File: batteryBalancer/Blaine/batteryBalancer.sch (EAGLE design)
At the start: 32 parts

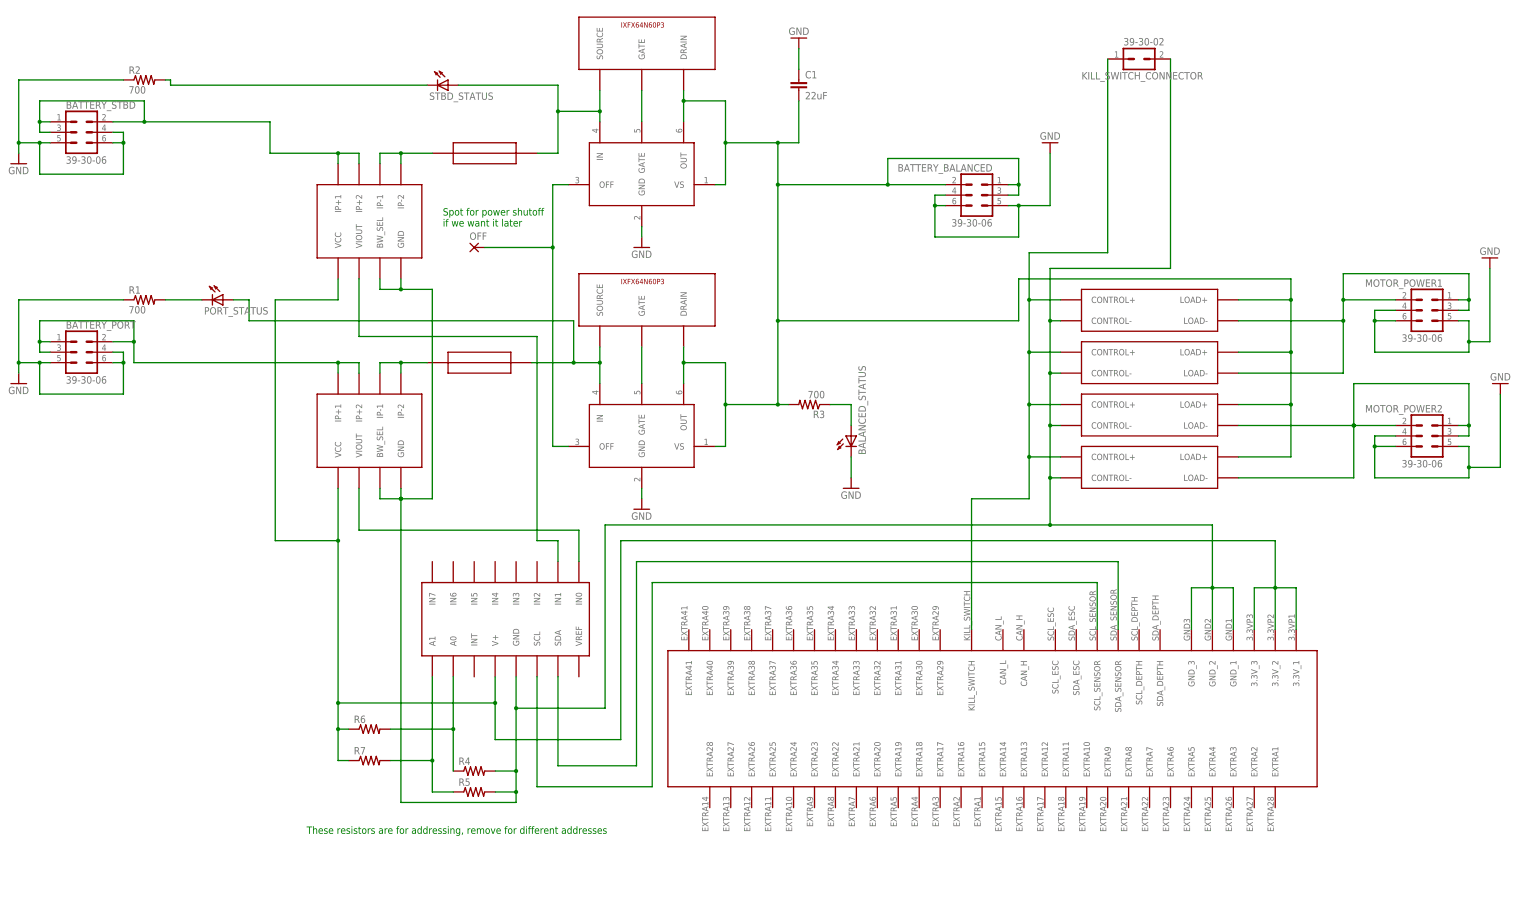
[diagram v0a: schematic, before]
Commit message: Routed the board
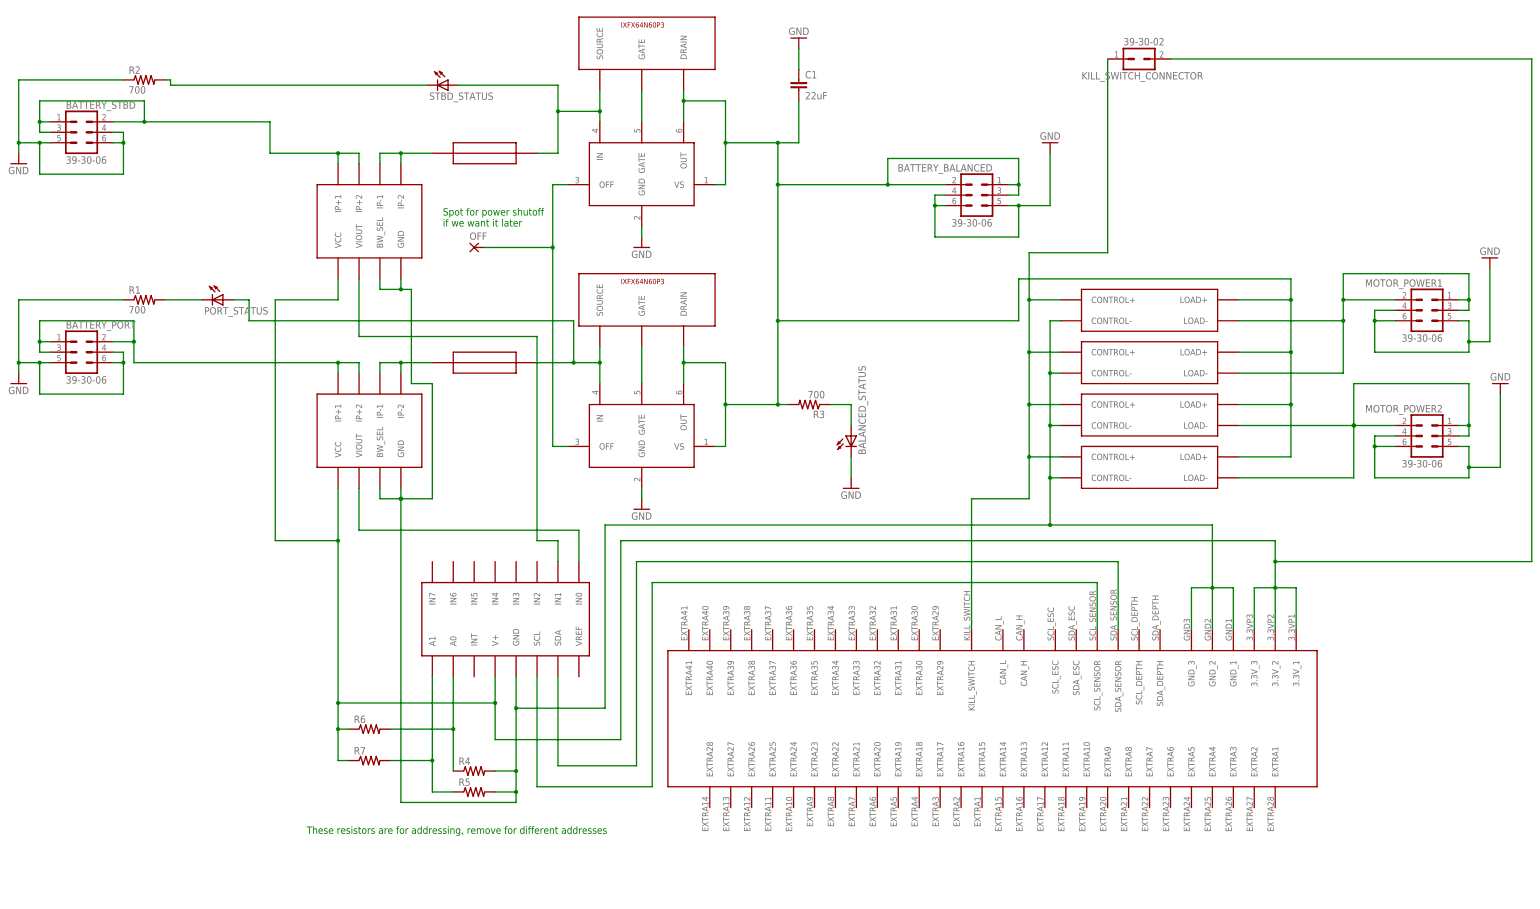
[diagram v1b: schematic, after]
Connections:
- net 3.3V: now also KILL_SWITCH_CONNECTOR.2
- net LOGIC_GND: no longer KILL_SWITCH_CONNECTOR.2
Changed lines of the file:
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@@
 <instance part="GND9" gate="1" x="396.24" y="149.86" rot="R180"/>
 <instance part="STBD_FUSE" gate="G$1" x="149.86" y="205.74"/>
-<instance part="PORT_FUSE" gate="G$1" x="148.59" y="154.94"/>
+<instance part="PORT_FUSE" gate="G$1" x="149.86" y="154.94"/>
 <instance part="ADC" gate="G$1" x="154.94" y="93.98"/>
 <instance part="R4" gate="G$1" x="147.32" y="55.88"/>
@@
 <junction x="157.48" y="55.88"/>
 <pinref part="PORT_CS" gate="G$1" pin="GND"/>
-<pinref part="STBD_CS" gate="G$1" pin="GND"/>
-<wire x1="129.54" y1="172.72" x2="129.54" y2="175.26" width="0.1524" layer="91"/>
-<pinref part="STBD_CS" gate="G$1" pin="BW_SEL"/>
-<wire x1="124.46" y1="175.26" x2="124.46" y2="172.72" width="0.1524" layer="91"/>
-<wire x1="124.46" y1="172.72" x2="129.54" y2="172.72" width="0.1524" layer="91"/>
-<junction x="129.54" y="172.72"/>
-<wire x1="137.16" y1="172.72" x2="129.54" y2="172.72" width="0.1524" layer="91"/>
-<wire x1="137.16" y1="121.92" x2="137.16" y2="172.72" width="0.1524" layer="91"/>
 <wire x1="157.48" y1="48.26" x2="129.54" y2="48.26" width="0.1524" layer="91"/>
 <wire x1="129.54" y1="48.26" x2="129.54" y2="121.92" width="0.1524" layer="91"/>
@@
 <wire x1="326.39" y1="115.57" x2="326.39" y2="100.33" width="0.1524" layer="91"/>
 <junction x="287.02" y="115.57"/>
-<wire x1="287.02" y1="165.1" x2="287.02" y2="177.8" width="0.1524" layer="91"/>
-<pinref part="KILL_SWITCH_CONNECTOR" gate="G$1" pin="2"/>
-<wire x1="287.02" y1="177.8" x2="316.23" y2="177.8" width="0.1524" layer="91"/>
-<wire x1="316.23" y1="177.8" x2="316.23" y2="228.6" width="0.1524" layer="91"/>
-<junction x="287.02" y="165.1"/>
+<wire x1="137.16" y1="121.92" x2="137.16" y2="149.86" width="0.1524" layer="91"/>
+<pinref part="STBD_CS" gate="G$1" pin="GND"/>
+<wire x1="129.54" y1="172.72" x2="129.54" y2="175.26" width="0.1524" layer="91"/>
+<junction x="129.54" y="172.72"/>
+<pinref part="STBD_CS" gate="G$1" pin="BW_SEL"/>
+<wire x1="132.08" y1="172.72" x2="129.54" y2="172.72" width="0.1524" layer="91"/>
+<wire x1="124.46" y1="175.26" x2="124.46" y2="172.72" width="0.1524" layer="91"/>
+<wire x1="124.46" y1="172.72" x2="129.54" y2="172.72" width="0.1524" layer="91"/>
+<wire x1="137.16" y1="149.86" x2="132.08" y2="149.86" width="0.1524" layer="91"/>
+<wire x1="132.08" y1="149.86" x2="132.08" y2="172.72" width="0.1524" layer="91"/>
 </segment>
 </net>
@@
 <wire x1="129.54" y1="154.94" x2="129.54" y2="152.4" width="0.1524" layer="91"/>
 <pinref part="PORT_FUSE" gate="G$1" pin="P$1"/>
-<wire x1="129.54" y1="154.94" x2="135.89" y2="154.94" width="0.1524" layer="91"/>
+<wire x1="129.54" y1="154.94" x2="137.16" y2="154.94" width="0.1524" layer="91"/>
 <junction x="129.54" y="154.94"/>
 </segment>
@@
 <wire x1="346.71" y1="100.33" x2="346.71" y2="90.17" width="0.1524" layer="91"/>
 <pinref part="EDGE_CONNECTOR" gate="G$1" pin="3.3V_2"/>
-<wire x1="341.63" y1="100.33" x2="341.63" y2="111.76" width="0.1524" layer="91"/>
+<wire x1="341.63" y1="100.33" x2="341.63" y2="106.68" width="0.1524" layer="91"/>
+<wire x1="341.63" y1="106.68" x2="341.63" y2="111.76" width="0.1524" layer="91"/>
 <wire x1="341.63" y1="100.33" x2="341.63" y2="90.17" width="0.1524" layer="91"/>
 <wire x1="341.63" y1="100.33" x2="346.71" y2="100.33" width="0.1524" layer="91"/>
@@
 <junction x="152.4" y="72.39"/>
 <junction x="114.3" y="72.39"/>
+<wire x1="341.63" y1="106.68" x2="403.86" y2="106.68" width="0.1524" layer="91"/>
+<wire x1="403.86" y1="106.68" x2="403.86" y2="228.6" width="0.1524" layer="91"/>
+<junction x="341.63" y="106.68"/>
+<pinref part="KILL_SWITCH_CONNECTOR" gate="G$1" pin="2"/>
+<wire x1="403.86" y1="228.6" x2="316.23" y2="228.6" width="0.1524" layer="91"/>
 </segment>
 </net>
@@
 <pinref part="PORT_FUSE" gate="G$1" pin="P$2"/>
 <wire x1="177.8" y1="154.94" x2="177.8" y2="149.86" width="0.1524" layer="91"/>
-<wire x1="161.29" y1="154.94" x2="171.45" y2="154.94" width="0.1524" layer="91"/>
+<wire x1="162.56" y1="154.94" x2="171.45" y2="154.94" width="0.1524" layer="91"/>
 <junction x="177.8" y="154.94"/>
 <pinref part="PORT_STATUS" gate="G$1" pin="A"/>

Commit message: Prettied up the routing and added kill switch indicator
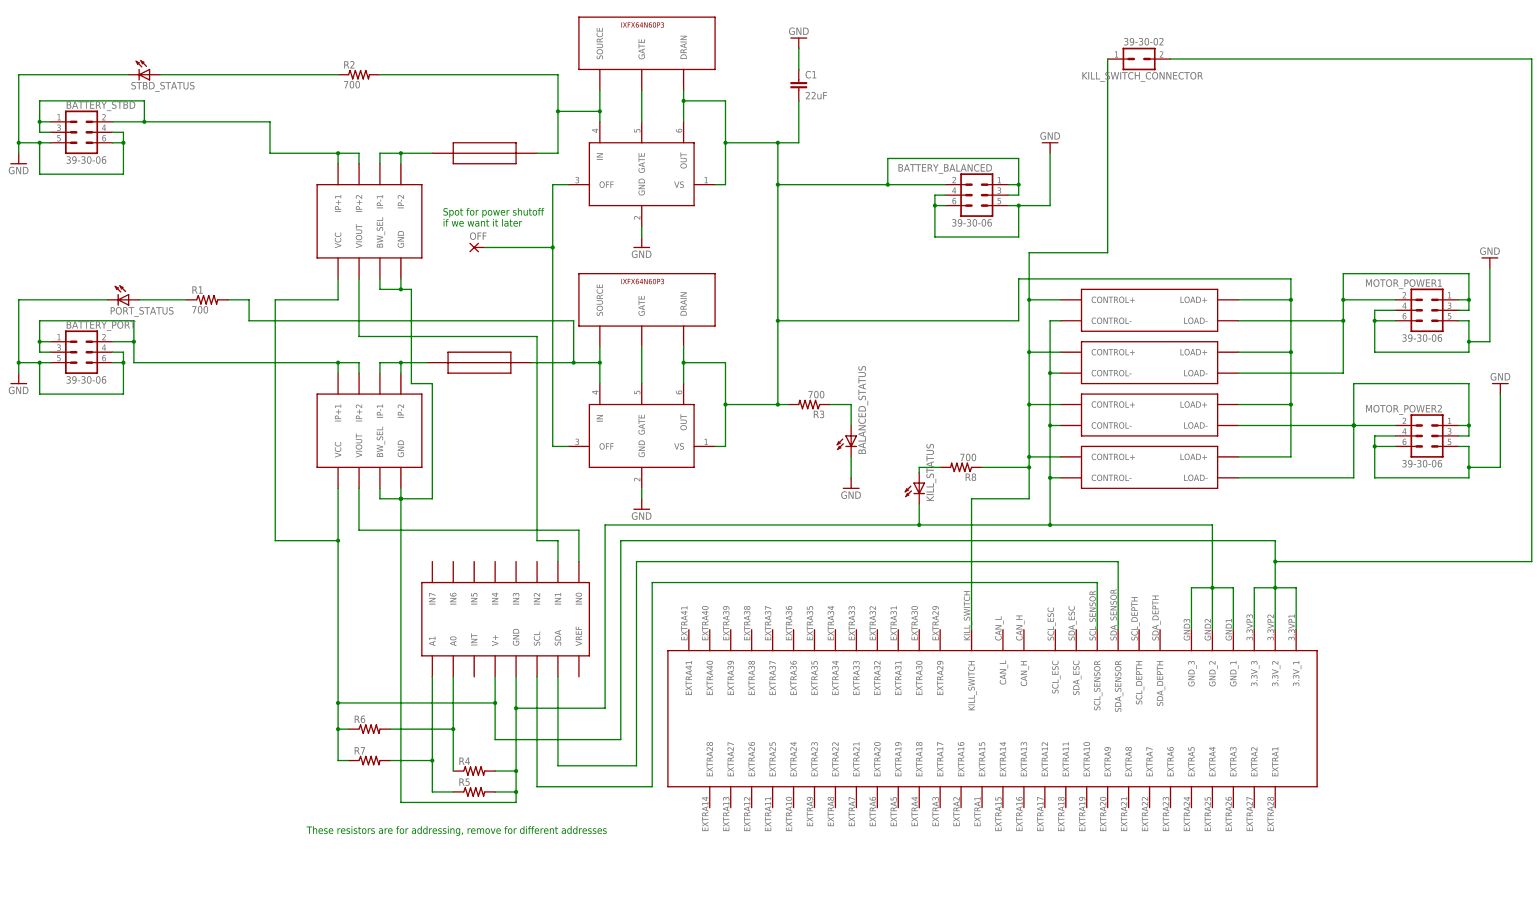
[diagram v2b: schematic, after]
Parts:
- added KILL_STATUS: LTST-S270GKT, LTST-S270GKT:LTST-S270GKT
- added R8: 700, rcl:R-US_0207/7
- R1, R2, R3: device rcl:R-US_MELF0204W -> rcl:R-US_0207/7
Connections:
- removed net PORT_INDICATOR: PORT_STATUS.C, R1.2
- removed net STBD_INDICATOR: R2.2, STBD_STATUS.C
- new net N$3: KILL_STATUS.A, R8.2
- new net PORT_STATUS: PORT_STATUS.A, R1.1
- new net STBD_STATUS: R2.1, STBD_STATUS.A
- net GND: now also PORT_STATUS.C, STBD_STATUS.C; no longer R1.1, R2.1
- net KILL_SWITCH: now also R8.1
- net LOGIC_GND: now also KILL_STATUS.C
- net N$1: now also R1.2; no longer PORT_STATUS.A
- net STBD_UNBALANCED: now also R2.2; no longer STBD_STATUS.A
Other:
- moved on the sheet: PORT_STATUS, R1, R2, STBD_STATUS

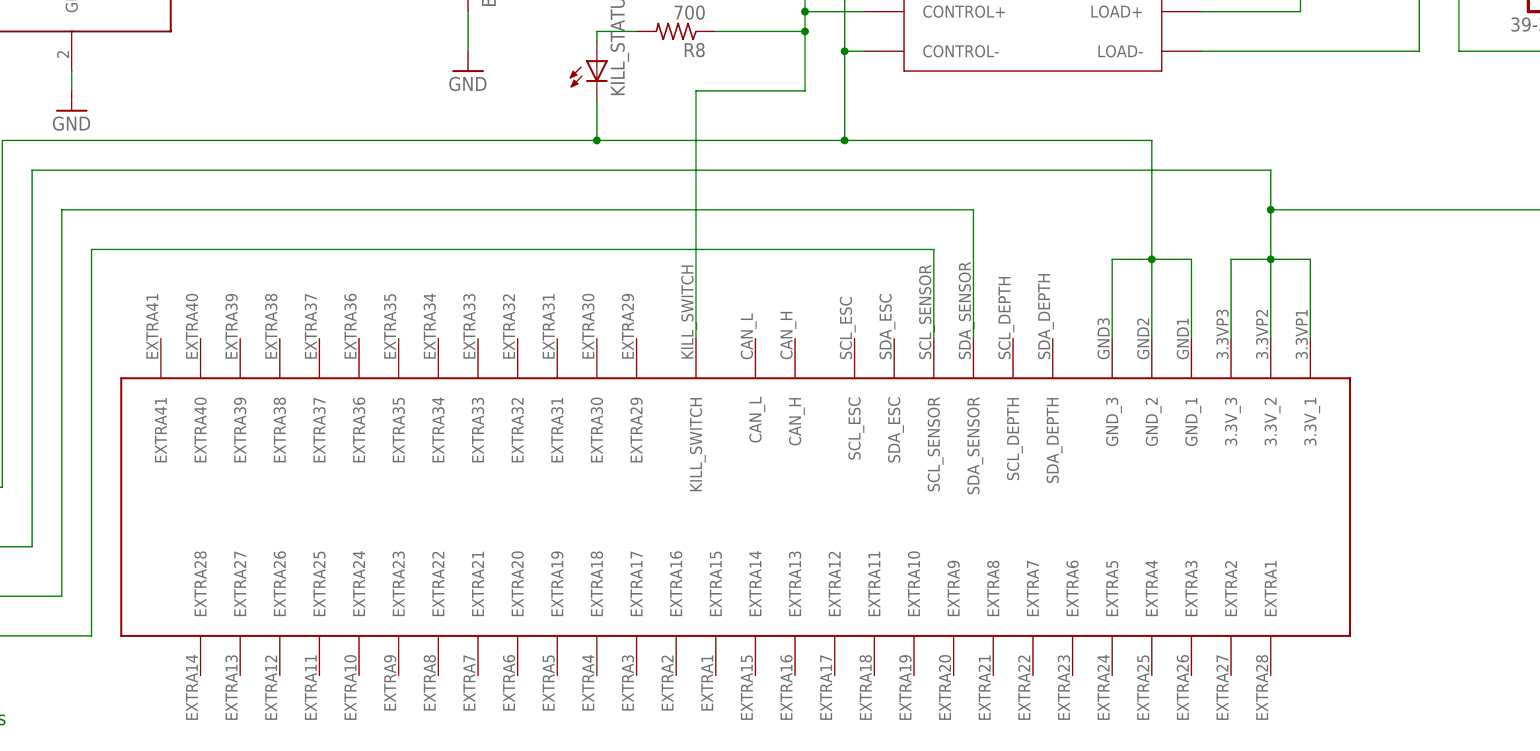
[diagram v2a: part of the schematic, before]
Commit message: Lost all my work :( but at least I got the new edge connector
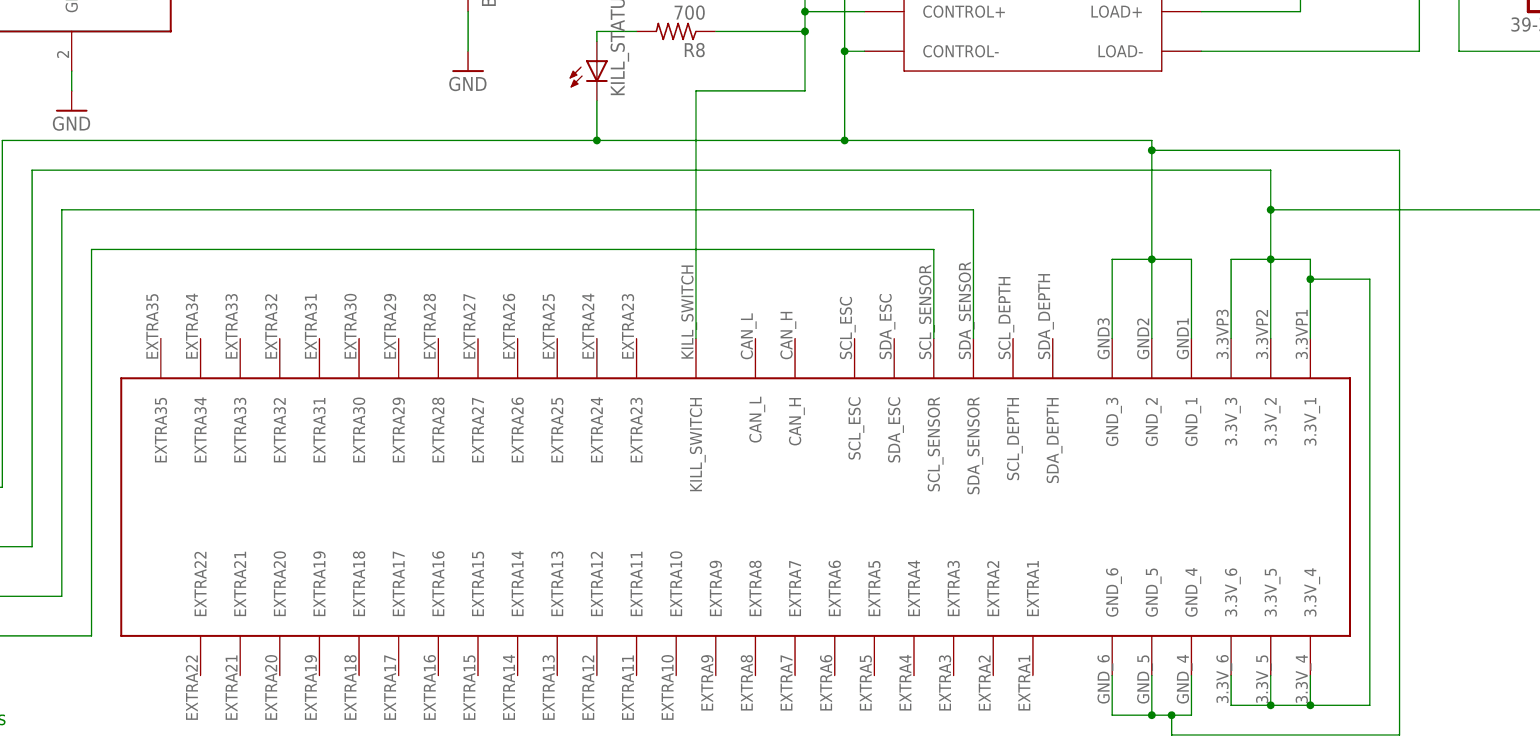
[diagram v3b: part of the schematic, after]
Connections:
- net 3.3V: now also EDGE_CONNECTOR.3.3V_4, EDGE_CONNECTOR.3.3V_5, EDGE_CONNECTOR.3.3V_6
- net LOGIC_GND: now also EDGE_CONNECTOR.GND_4, EDGE_CONNECTOR.GND_5, EDGE_CONNECTOR.GND_6
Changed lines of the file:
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@@
 <wire x1="255.27" y1="115.57" x2="287.02" y2="115.57" width="0.1524" layer="91"/>
 <wire x1="287.02" y1="115.57" x2="326.39" y2="115.57" width="0.1524" layer="91"/>
-<wire x1="326.39" y1="115.57" x2="326.39" y2="100.33" width="0.1524" layer="91"/>
+<wire x1="326.39" y1="115.57" x2="326.39" y2="114.3" width="0.1524" layer="91"/>
 <junction x="287.02" y="115.57"/>
+<wire x1="326.39" y1="114.3" x2="326.39" y2="100.33" width="0.1524" layer="91"/>
 <wire x1="137.16" y1="121.92" x2="137.16" y2="149.86" width="0.1524" layer="91"/>
 <pinref part="STBD_CS" gate="G$1" pin="GND"/>
@@
 <wire x1="255.27" y1="120.65" x2="255.27" y2="115.57" width="0.1524" layer="91"/>
 <junction x="255.27" y="115.57"/>
+<pinref part="EDGE_CONNECTOR" gate="G$1" pin="GND_6"/>
+<wire x1="321.31" y1="46.99" x2="321.31" y2="41.91" width="0.1524" layer="91"/>
+<pinref part="EDGE_CONNECTOR" gate="G$1" pin="GND_4"/>
+<wire x1="321.31" y1="41.91" x2="326.39" y2="41.91" width="0.1524" layer="91"/>
+<wire x1="326.39" y1="41.91" x2="328.93" y2="41.91" width="0.1524" layer="91"/>
+<wire x1="328.93" y1="41.91" x2="331.47" y2="41.91" width="0.1524" layer="91"/>
+<wire x1="331.47" y1="41.91" x2="331.47" y2="46.99" width="0.1524" layer="91"/>
+<pinref part="EDGE_CONNECTOR" gate="G$1" pin="GND_5"/>
+<wire x1="326.39" y1="46.99" x2="326.39" y2="41.91" width="0.1524" layer="91"/>
+<junction x="326.39" y="41.91"/>
+<wire x1="328.93" y1="41.91" x2="328.93" y2="39.37" width="0.1524" layer="91"/>
+<junction x="328.93" y="41.91"/>
+<wire x1="328.93" y1="39.37" x2="358.14" y2="39.37" width="0.1524" layer="91"/>
+<wire x1="358.14" y1="39.37" x2="358.14" y2="114.3" width="0.1524" layer="91"/>
+<wire x1="358.14" y1="114.3" x2="326.39" y2="114.3" width="0.1524" layer="91"/>
+<junction x="326.39" y="114.3"/>
 </segment>
 </net>
@@
 <wire x1="182.88" y1="63.5" x2="182.88" y2="111.76" width="0.1524" layer="91"/>
 <pinref part="EDGE_CONNECTOR" gate="G$1" pin="3.3V_1"/>
-<wire x1="346.71" y1="100.33" x2="346.71" y2="90.17" width="0.1524" layer="91"/>
+<wire x1="346.71" y1="100.33" x2="346.71" y2="97.79" width="0.1524" layer="91"/>
 <pinref part="EDGE_CONNECTOR" gate="G$1" pin="3.3V_2"/>
+<wire x1="346.71" y1="97.79" x2="346.71" y2="90.17" width="0.1524" layer="91"/>
 <wire x1="341.63" y1="100.33" x2="341.63" y2="106.68" width="0.1524" layer="91"/>
 <wire x1="341.63" y1="106.68" x2="341.63" y2="111.76" width="0.1524" layer="91"/>
@@
 <pinref part="KILL_SWITCH_CONNECTOR" gate="G$1" pin="2"/>
 <wire x1="403.86" y1="228.6" x2="316.23" y2="228.6" width="0.1524" layer="91"/>
+<pinref part="EDGE_CONNECTOR" gate="G$1" pin="3.3V_6"/>
+<wire x1="336.55" y1="46.99" x2="336.55" y2="43.18" width="0.1524" layer="91"/>
+<pinref part="EDGE_CONNECTOR" gate="G$1" pin="3.3V_4"/>
+<wire x1="336.55" y1="43.18" x2="341.63" y2="43.18" width="0.1524" layer="91"/>
+<wire x1="341.63" y1="43.18" x2="346.71" y2="43.18" width="0.1524" layer="91"/>
+<wire x1="346.71" y1="43.18" x2="346.71" y2="46.99" width="0.1524" layer="91"/>
+<pinref part="EDGE_CONNECTOR" gate="G$1" pin="3.3V_5"/>
+<wire x1="341.63" y1="46.99" x2="341.63" y2="43.18" width="0.1524" layer="91"/>
+<junction x="341.63" y="43.18"/>
+<wire x1="346.71" y1="43.18" x2="354.33" y2="43.18" width="0.1524" layer="91"/>
+<wire x1="354.33" y1="43.18" x2="354.33" y2="97.79" width="0.1524" layer="91"/>
+<junction x="346.71" y="43.18"/>
+<wire x1="354.33" y1="97.79" x2="346.71" y2="97.79" width="0.1524" layer="91"/>
+<junction x="346.71" y="97.79"/>
 </segment>
 </net>
